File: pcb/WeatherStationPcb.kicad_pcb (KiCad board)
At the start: 2 copper layers, 37.8 x 19.1 mm, 7 parts, among them J1 Screw_Terminal_01x02, J2 Conn_01x06, J3 Conn_01x04, U1 MCP1755S-3302xCB, U3 ESP-01

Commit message: feat(pcb): update pcb
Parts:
- C1: value 100nF -> 10nF
- C2: value 10uF -> 10nF
- J2: value Conn_01x06 -> BME280
- J3: value Conn_01x04 -> BMP280
- moved J3 7.50 mm to (95.4, 60.2), turned to 270 degrees
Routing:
- net /SDA: track 31.9 -> 23.7 mm
- net /SCL: track 23.3 -> 20.6 mm
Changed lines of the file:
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@@
     (title WeatherStation)
     (date 2020-05-16)
-    (rev 2)
+    (rev 3)
   )
   (layers
@@
     (add_net /SCL)
     (add_net /SDA)
+    (add_net "Net-(J2-Pad5)")
+    (add_net "Net-(U3-Pad1)")
+    (add_net "Net-(U3-Pad5)")
+    (add_net "Net-(U3-Pad7)")
   )
   (net_class Power ""
@@
       (effects (font (size 1 1) (thickness 0.15)))
     )
-    (fp_text value 100nF (at 0 1.65) (layer F.Fab)
+    (fp_text value 10nF (at 0 1.65) (layer F.Fab)
       (effects (font (size 1 1) (thickness 0.15)))
     )
@@
       (effects (font (size 1 1) (thickness 0.15)))
     )
-    (fp_text value 10uF (at 0 1.65) (layer F.Fab)
+    (fp_text value 10nF (at 0 1.65) (layer F.Fab)
       (effects (font (size 1 1) (thickness 0.15)))
     )
@@
   )
   (module Connector_PinSocket_2.54mm:PinSocket_1x06_P2.54mm_Vertical (layer F.Cu)
-    (at 84.074 60.198 270)
+    (at 84.074 60.20054 270)
     (descr "Through hole straight socket strip, 1x06, 2.54mm pitch, single row (from Kicad 4.0.7), script generated")
     (tags "Through hole socket strip THT 1x06 2.54mm single row")
@@
       (effects (font (size 1 1) (thickness 0.15)))
     )
-    (fp_text value Conn_01x06 (at 0 15.47 90) (layer F.Fab)
+    (fp_text value BME280 (at 0 15.47 90) (layer F.Fab)
       (effects (font (size 1 1) (thickness 0.15)))
     )
@@
   )
   (module Connector_PinSocket_2.54mm:PinSocket_1x04_P2.54mm_Vertical (layer F.Cu)
-    (at 87.884 60.148 90)
+    (at 95.37954 60.20054 270)
     (descr "Through hole straight socket strip, 1x04, 2.54mm pitch, single row (from Kicad 4.0.7), script generated")
     (tags "Through hole socket strip THT 1x04 2.54mm single row")
-    (fp_text reference J3 (at 2.236 -1.27 180) (layer F.SilkS)
-      (effects (font (size 1 1) (thickness 0.15)))
-    )
-    (fp_text value Conn_01x04 (at 0 10.39 90) (layer F.Fab)
+    (fp_text reference J3 (at -2.44094 8.47598 180) (layer F.SilkS)
+      (effects (font (size 1 1) (thickness 0.15)))
+    )
+    (fp_text value BMP280 (at 0 10.39 90) (layer F.Fab)
       (effects (font (size 1 1) (thickness 0.15)))
     )
@@
       (effects (font (size 1 1) (thickness 0.15)))
     )
-    (pad 1 thru_hole rect (at 0 0 90) (size 1.7 1.7) (drill 1) (layers *.Cu *.Mask)
-      (net 5 /VCC))
-    (pad 2 thru_hole oval (at 0 2.54 90) (size 1.7 1.7) (drill 1) (layers *.Cu *.Mask)
-      (net 1 GND))
-    (pad 3 thru_hole oval (at 0 5.08 90) (size 1.7 1.7) (drill 1) (layers *.Cu *.Mask)
+    (pad 1 thru_hole rect (at 0 0 270) (size 1.7 1.7) (drill 1) (layers *.Cu *.Mask)
+      (net 5 /VCC))
+    (pad 2 thru_hole oval (at 0 2.54 270) (size 1.7 1.7) (drill 1) (layers *.Cu *.Mask)
+      (net 1 GND))
+    (pad 3 thru_hole oval (at 0 5.08 270) (size 1.7 1.7) (drill 1) (layers *.Cu *.Mask)
       (net 3 /SCL))
-    (pad 4 thru_hole oval (at 0 7.62 90) (size 1.7 1.7) (drill 1) (layers *.Cu *.Mask)
+    (pad 4 thru_hole oval (at 0 7.62 270) (size 1.7 1.7) (drill 1) (layers *.Cu *.Mask)
       (net 4 /SDA))
     (model ${KISYS3DMOD}/Connector_PinSocket_2.54mm.3dshapes/PinSocket_1x04_P2.54mm_Vertical.wrl
@@
   (gr_line (start 96.774 63.754) (end 60.96 63.754) (layer Edge.Cuts) (width 0.05))
   (segment (start 73.152 55.372) (end 73.152 55.118) (width 0.5) (layer F.Cu) (net 1))
-  (segment (start 72.136 56.388) (end 73.152 55.372) (width 0.5) (layer F.Cu) (net 1))
-  (segment (start 73.152 55.136) (end 73.152 53.442) (width 0.5) (layer F.Cu) (net 1))
-  (segment (start 74.404 56.388) (end 73.152 55.136) (width 0.5) (layer F.Cu) (net 1))
-  (segment (start 73.152 55.118) (end 73.152 53.442) (width 0.5) (layer F.Cu) (net 1))
+  (segment (start 72.136 56.388) (end 73.152 55.372) (width 0.5) (layer F.Cu) (net 1) (status 10))
+  (segment (start 73.152 55.136) (end 73.152 53.442) (width 0.5) (layer F.Cu) (net 1) (status 20))
+  (segment (start 74.404 56.388) (end 73.152 55.136) (width 0.5) (layer F.Cu) (net 1) (status 10))
+  (segment (start 73.152 55.118) (end 73.152 53.442) (width 0.5) (layer F.Cu) (net 1) (status 20))
   (via (at 73.152 55.118) (size 0.8) (drill 0.4) (layers F.Cu B.Cu) (net 1))
-  (segment (start 70.086 57.088) (end 70.086 56.388) (width 0.5) (layer F.Cu) (net 2))
+  (segment (start 70.086 57.088) (end 70.086 56.388) (width 0.5) (layer F.Cu) (net 2) (status 20))
   (segment (start 67.865 59.309) (end 70.086 57.088) (width 0.5) (layer F.Cu) (net 2))
-  (segment (start 64.643 59.309) (end 67.865 59.309) (width 0.5) (layer F.Cu) (net 2))
-  (segment (start 70.086 54.208) (end 70.852 53.442) (width 0.5) (layer F.Cu) (net 2))
-  (segment (start 70.086 56.388) (end 70.086 54.208) (width 0.5) (layer F.Cu) (net 2))
-  (segment (start 78.994 60.198) (end 78.994 58.674) (width 0.25) (layer F.Cu) (net 3))
+  (segment (start 64.643 59.309) (end 67.865 59.309) (width 0.5) (layer F.Cu) (net 2) (status 10))
+  (segment (start 70.086 54.208) (end 70.852 53.442) (width 0.5) (layer F.Cu) (net 2) (status 20))
+  (segment (start 70.086 56.388) (end 70.086 54.208) (width 0.5) (layer F.Cu) (net 2) (status 10))
+  (segment (start 78.994 60.198) (end 78.994 58.674) (width 0.25) (layer F.Cu) (net 3) (status 10))
   (segment (start 78.994 58.674) (end 78.486 58.166) (width 0.25) (layer F.Cu) (net 3))
-  (segment (start 78.486 54.356) (end 80.01 52.832) (width 0.25) (layer F.Cu) (net 3))
+  (segment (start 78.486 54.356) (end 80.01 52.832) (width 0.25) (layer F.Cu) (net 3) (status 20))
   (segment (start 78.486 58.166) (end 78.486 54.356) (width 0.25) (layer F.Cu) (net 3))
-  (segment (start 92.114001 60.997999) (end 92.964 60.148) (width 0.25) (layer F.Cu) (net 3))
-  (segment (start 91.638999 61.473001) (end 92.114001 60.997999) (width 0.25) (layer F.Cu) (net 3))
-  (segment (start 80.269001 61.473001) (end 91.638999 61.473001) (width 0.25) (layer F.Cu) (net 3))
-  (segment (start 78.994 60.198) (end 80.269001 61.473001) (width 0.25) (layer F.Cu) (net 3))
-  (segment (start 80.01 50.292) (end 77.978 52.324) (width 0.25) (layer F.Cu) (net 4))
-  (segment (start 77.978 58.674) (end 76.454 60.198) (width 0.25) (layer F.Cu) (net 4))
+  (segment (start 89.449541 61.050539) (end 90.29954 60.20054) (width 0.25) (layer B.Cu) (net 3) (status 20))
+  (segment (start 89.024539 61.475541) (end 89.449541 61.050539) (width 0.25) (layer B.Cu) (net 3))
+  (segment (start 80.269001 61.475541) (end 89.024539 61.475541) (width 0.25) (layer B.Cu) (net 3))
+  (segment (start 78.994 60.20054) (end 80.269001 61.475541) (width 0.25) (layer B.Cu) (net 3) (status 10))
+  (segment (start 80.01 50.292) (end 77.978 52.324) (width 0.25) (layer F.Cu) (net 4) (status 10))
+  (segment (start 77.978 58.674) (end 76.454 60.198) (width 0.25) (layer F.Cu) (net 4) (status 20))
   (segment (start 77.978 52.324) (end 77.978 58.674) (width 0.25) (layer F.Cu) (net 4))
-  (segment (start 94.654001 60.997999) (end 95.504 60.148) (width 0.25) (layer F.Cu) (net 4))
-  (segment (start 93.72899 61.92301) (end 94.654001 60.997999) (width 0.25) (layer F.Cu) (net 4))
-  (segment (start 78.17901 61.92301) (end 93.72899 61.92301) (width 0.25) (layer F.Cu) (net 4))
-  (segment (start 76.454 60.198) (end 78.17901 61.92301) (width 0.25) (layer F.Cu) (net 4))
+  (segment (start 86.909541 61.050539) (end 87.75954 60.20054) (width 0.25) (layer F.Cu) (net 4) (status 20))
+  (segment (start 86.484539 61.475541) (end 86.909541 61.050539) (width 0.25) (layer F.Cu) (net 4))
+  (segment (start 77.729001 61.475541) (end 86.484539 61.475541) (width 0.25) (layer F.Cu) (net 4))
+  (segment (start 76.454 60.20054) (end 77.729001 61.475541) (width 0.25) (layer F.Cu) (net 4) (status 10))
   (zone (net 5) (net_name /VCC) (layer F.Cu) (hatch edge 0.508)
     (connect_pads (clearance 0.508))

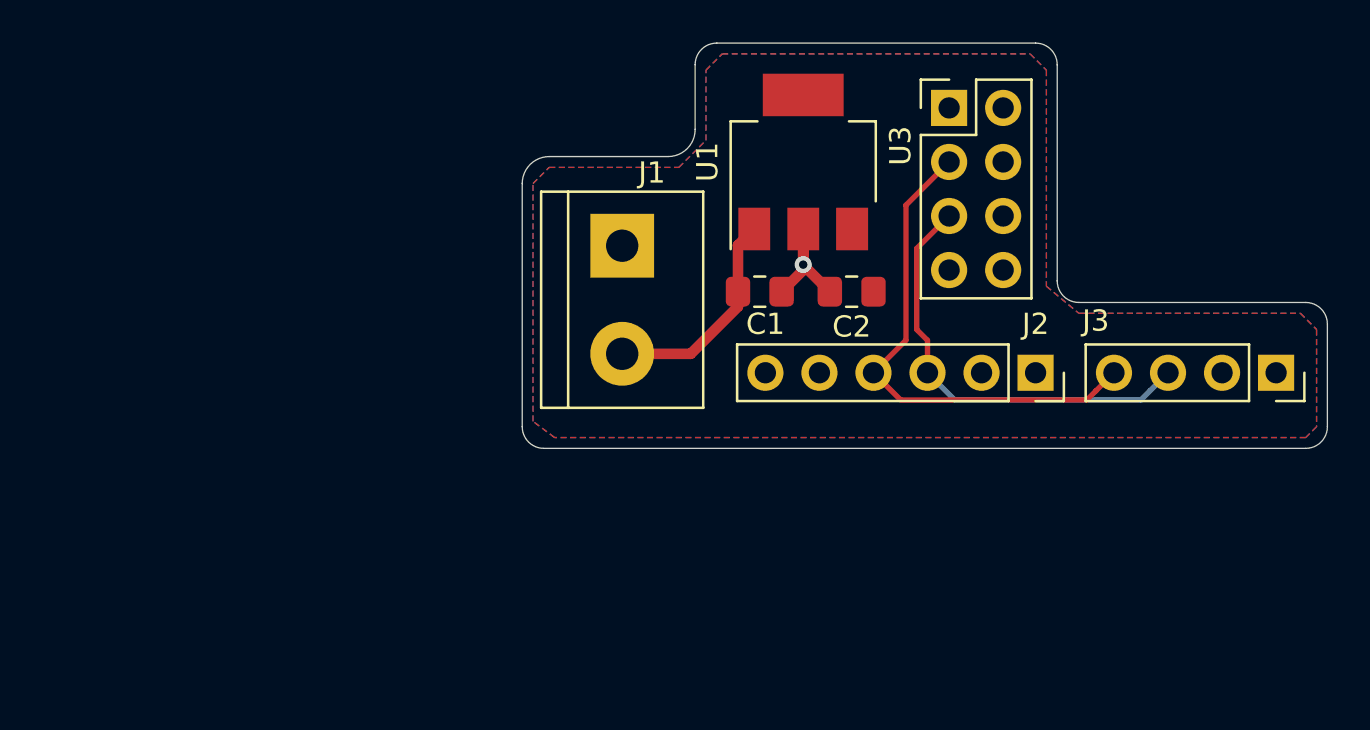
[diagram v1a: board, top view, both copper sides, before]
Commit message: feat(pcb): update the pcb by adding voltage sensor
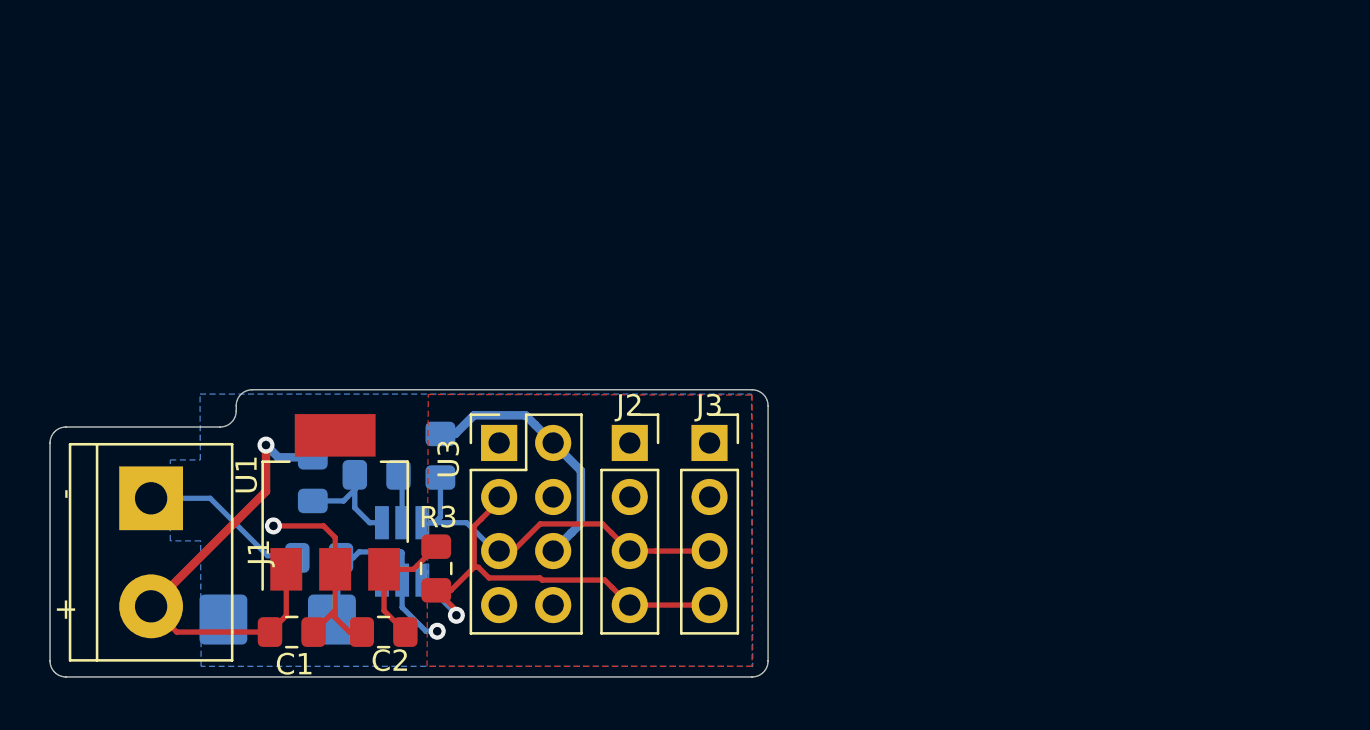
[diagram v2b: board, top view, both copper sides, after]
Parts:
- added C3: 10u, Capacitor_Tantalum_SMD:CP_EIA-6032-28_Kemet-C_Pad2.25x2.35mm_HandSolder, B.Cu at (48.5, 71.8)
- added C4: 0.1u, Capacitor_SMD:C_0805_2012Metric_Pad1.15x1.40mm_HandSolder, B.Cu at (50.4, 68.9)
- added R1: 10M, Resistor_SMD:R_0805_2012Metric_Pad1.15x1.40mm_HandSolder, B.Cu at (50.1, 65.2)
- added R2: 2,7M, Resistor_SMD:R_0805_2012Metric_Pad1.15x1.40mm_HandSolder, B.Cu at (53.1, 65.0)
- added R3: 10k, Resistor_SMD:R_0805_2012Metric_Pad1.15x1.40mm_HandSolder, F.Cu at (55.9, 69.4)
- added R4: 10k, Resistor_SMD:R_0805_2012Metric_Pad1.15x1.40mm_HandSolder, B.Cu at (56.1, 64.1)
- added U2: MCP3421A0T-ECH, Package_TO_SOT_SMD:SOT-23-6_Handsoldering, B.Cu at (54.3, 68.6)
- C1, C2: value 10nF -> 1uF
- J2: footprint Connector_PinSocket_2.54mm:PinSocket_1x06_P2.54mm_Vertical -> Connector_PinSocket_2.54mm:PinSocket_1x04_P2.54mm_Vertical
- moved C1 27.2 mm to (49.1, 72.4)
- moved C2 27.2 mm to (53.4, 72.4)
- moved U1 27.2 mm to (51.2, 66.3)
- moved J3 26.8 mm to (68.8, 63.5), turned to 0 degrees
- moved U3 26.4 mm to (61.4, 63.5)
- moved J1 25.1 mm to (42.5, 66.1)
- moved J2 19.4 mm to (65.0, 63.5), turned to 0 degrees
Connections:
- net Net-(C1-Pad1) renamed VCC
- C2 pad 1: /VCC -> /3V3
- J2 pad 1: /VCC -> /3V3
- J3 pad 1: /VCC -> /3V3
- U1 pad 3: /VCC -> /3V3
- U3 pad 6: /VCC -> /3V3
- U3 pad 8: /VCC -> /3V3
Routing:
- net /3V3: track 0.00 -> 29.1 mm, vias 0 -> 1
- net GND: track 6.83 -> 20.2 mm
- net VCC: track 10.3 -> 21.6 mm, vias 0 -> 1
- net Net-(R1-Pad2): track 0.00 -> 6.01 mm
- net /SCL: track 20.6 -> 18.0 mm
- net /SDA: track 23.7 -> 21.5 mm, vias 0 -> 1
- added copper zone on F.Cu, net /3V3
- removed copper zone on F.Cu, net /VCC
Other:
- board size 37.8 x 19.1 mm -> 33.8 x 13.5 mm
- net class Power: clearance 0.3 -> 0.25; trace_width 0.5 -> 0.4
- board text added: "+"
- board text added: "-"
- board text added: "REV 4"
